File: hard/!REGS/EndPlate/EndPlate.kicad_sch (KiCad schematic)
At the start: 10 parts, among them J1 Conn_01x13_Socket, J2 Conn_01x13_Socket, J3 Conn_01x13_Socket, J4 Conn_01x13_Socket, J5 Conn_01x13_Socket, J6 Conn_01x13_Socket, J7 Conn_01x13_Socket, J8 Conn_01x13_Socket, U1 74HC245, U2 74HC245

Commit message: End Plate PCB in work
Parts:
- added J10, J9: Conn_01x03_Pin, Connector_PinHeader_2.54mm:PinHeader_1x03_P2.54mm_Vertical, symbol Connector:Conn_01x03_Pin
- J1, J2, J3, J4, J5, J6, J7, J8: footprint Connector_PinSocket_2.54mm:PinSocket_1x13_P2.54mm_Vertical -> Connector_PinSocket_2.54mm:PinSocket_1x13_P2.54mm_Vertical_SMD_Pin1Left
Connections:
- net DST0: now also J1.11 (Pin_11); no longer J1.6 (Pin_6)
- net DST1: now also J2.11 (Pin_11); no longer J2.6 (Pin_6)
- net DST2: now also J3.11 (Pin_11); no longer J3.6 (Pin_6)
- net DST3: now also J4.11 (Pin_11); no longer J4.6 (Pin_6)
- net DST4: now also J5.11 (Pin_11); no longer J5.6 (Pin_6)
- net DST5: now also J6.11 (Pin_11); no longer J6.6 (Pin_6)
- net DST6: now also J7.11 (Pin_11); no longer J7.6 (Pin_6)
- net DST7: now also J8.11 (Pin_11); no longer J8.6 (Pin_6)
- net S0.0: now also J9.1 (Pin_1)
- net S0.1: now also J9.2 (Pin_2)
- net S0.2: now also J9.3 (Pin_3)
- net S1.0: now also J1.6 (Pin_6), J2.6 (Pin_6), J3.6 (Pin_6), J4.6 (Pin_6), J5.6 (Pin_6), J6.6 (Pin_6), J7.6 (Pin_6), J8.6 (Pin_6), J10.1 (Pin_1); no longer J1.8 (Pin_8), J2.8 (Pin_8), J3.8 (Pin_8), J4.8 (Pin_8), J5.8 (Pin_8), J6.8 (Pin_8), J7.8 (Pin_8), J8.8 (Pin_8)
- net S1.1: now also J1.7 (Pin_7), J2.7 (Pin_7), J3.7 (Pin_7), J4.7 (Pin_7), J5.7 (Pin_7), J6.7 (Pin_7), J7.7 (Pin_7), J8.7 (Pin_7), J10.2 (Pin_2); no longer J1.9 (Pin_9), J2.9 (Pin_9), J3.9 (Pin_9), J4.9 (Pin_9), J5.9 (Pin_9), J6.9 (Pin_9), J7.9 (Pin_9), J8.9 (Pin_9)
- net S1.2: now also J1.8 (Pin_8), J2.8 (Pin_8), J3.8 (Pin_8), J4.8 (Pin_8), J5.8 (Pin_8), J6.8 (Pin_8), J7.8 (Pin_8), J8.8 (Pin_8), J10.3 (Pin_3); no longer J1.10 (Pin_10), J2.10 (Pin_10), J3.10 (Pin_10), J4.10 (Pin_10), J5.10 (Pin_10), J6.10 (Pin_10), J7.10 (Pin_10), J8.10 (Pin_10)
- net ~E1: now also J1.9 (Pin_9), J2.9 (Pin_9), J3.9 (Pin_9), J4.9 (Pin_9), J5.9 (Pin_9), J6.9 (Pin_9), J7.9 (Pin_9), J8.9 (Pin_9); no longer J1.11 (Pin_11), J2.11 (Pin_11), J3.11 (Pin_11), J4.11 (Pin_11), J5.11 (Pin_11), J6.11 (Pin_11), J7.11 (Pin_11), J8.11 (Pin_11)

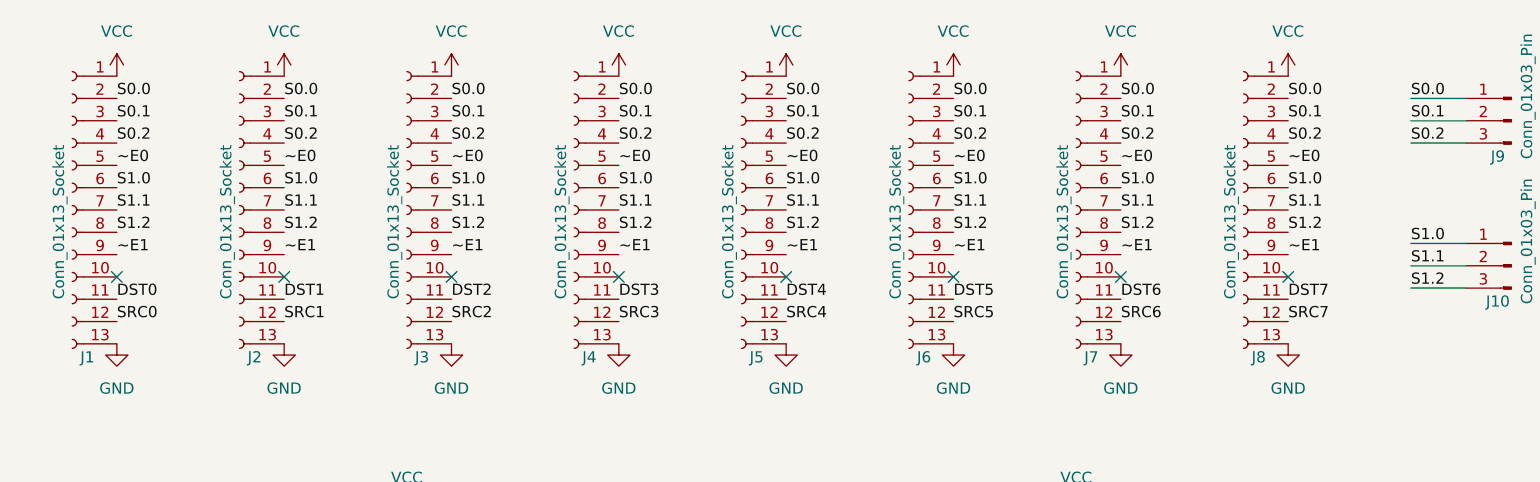
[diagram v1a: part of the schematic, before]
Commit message: End Plate: make a circuit corresponding to the multiplexers
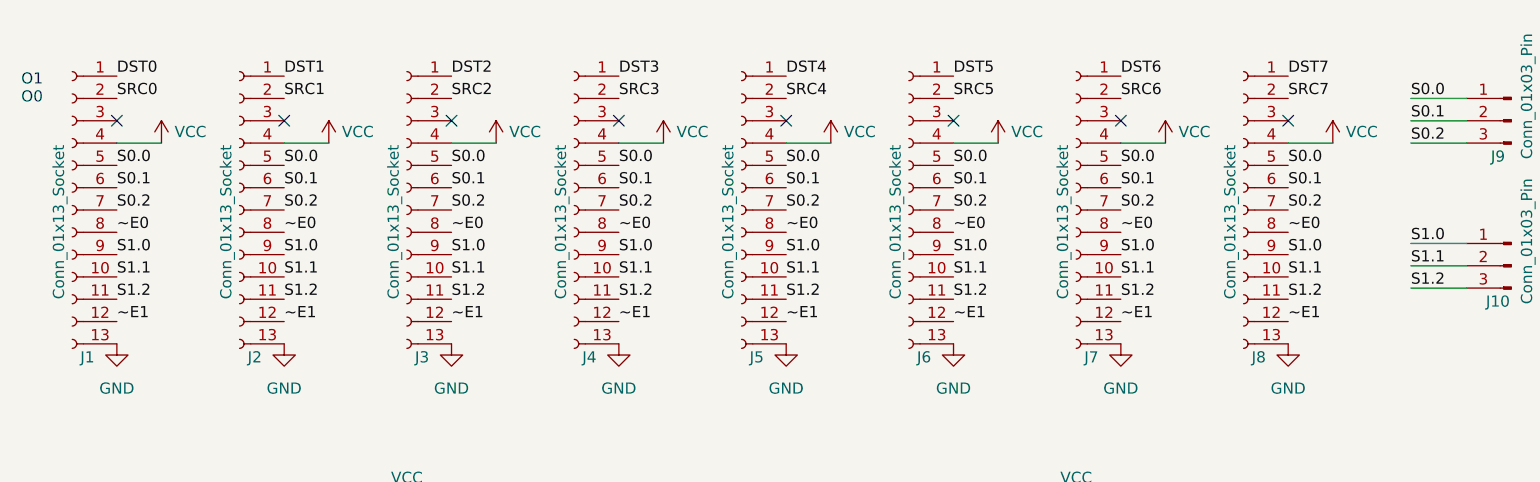
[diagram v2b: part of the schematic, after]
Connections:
- net DST0: now also J1.1 (Pin_1); no longer J1.11 (Pin_11)
- net DST1: now also J2.1 (Pin_1); no longer J2.11 (Pin_11)
- net DST2: now also J3.1 (Pin_1); no longer J3.11 (Pin_11)
- net DST3: now also J4.1 (Pin_1); no longer J4.11 (Pin_11)
- net DST4: now also J5.1 (Pin_1); no longer J5.11 (Pin_11)
- net DST5: now also J6.1 (Pin_1); no longer J6.11 (Pin_11)
- net DST6: now also J7.1 (Pin_1); no longer J7.11 (Pin_11)
- net DST7: now also J8.1 (Pin_1); no longer J8.11 (Pin_11)
- net S0.0: now also J1.5 (Pin_5), J2.5 (Pin_5), J3.5 (Pin_5), J4.5 (Pin_5), J5.5 (Pin_5), J6.5 (Pin_5), J7.5 (Pin_5), J8.5 (Pin_5); no longer J1.2 (Pin_2), J2.2 (Pin_2), J3.2 (Pin_2), J4.2 (Pin_2), J5.2 (Pin_2), J6.2 (Pin_2), J7.2 (Pin_2), J8.2 (Pin_2)
- net S0.1: now also J1.6 (Pin_6), J2.6 (Pin_6), J3.6 (Pin_6), J4.6 (Pin_6), J5.6 (Pin_6), J6.6 (Pin_6), J7.6 (Pin_6), J8.6 (Pin_6); no longer J1.3 (Pin_3), J2.3 (Pin_3), J3.3 (Pin_3), J4.3 (Pin_3), J5.3 (Pin_3), J6.3 (Pin_3), J7.3 (Pin_3), J8.3 (Pin_3)
- net S0.2: now also J1.7 (Pin_7), J2.7 (Pin_7), J3.7 (Pin_7), J4.7 (Pin_7), J5.7 (Pin_7), J6.7 (Pin_7), J7.7 (Pin_7), J8.7 (Pin_7); no longer J1.4 (Pin_4), J2.4 (Pin_4), J3.4 (Pin_4), J4.4 (Pin_4), J5.4 (Pin_4), J6.4 (Pin_4), J7.4 (Pin_4), J8.4 (Pin_4)
- net S1.0: now also J1.9 (Pin_9), J2.9 (Pin_9), J3.9 (Pin_9), J4.9 (Pin_9), J5.9 (Pin_9), J6.9 (Pin_9), J7.9 (Pin_9), J8.9 (Pin_9); no longer J1.6 (Pin_6), J2.6 (Pin_6), J3.6 (Pin_6), J4.6 (Pin_6), J5.6 (Pin_6), J6.6 (Pin_6), J7.6 (Pin_6), J8.6 (Pin_6)
- net S1.1: now also J1.10 (Pin_10), J2.10 (Pin_10), J3.10 (Pin_10), J4.10 (Pin_10), J5.10 (Pin_10), J6.10 (Pin_10), J7.10 (Pin_10), J8.10 (Pin_10); no longer J1.7 (Pin_7), J2.7 (Pin_7), J3.7 (Pin_7), J4.7 (Pin_7), J5.7 (Pin_7), J6.7 (Pin_7), J7.7 (Pin_7), J8.7 (Pin_7)
- net S1.2: now also J1.11 (Pin_11), J2.11 (Pin_11), J3.11 (Pin_11), J4.11 (Pin_11), J5.11 (Pin_11), J6.11 (Pin_11), J7.11 (Pin_11), J8.11 (Pin_11); no longer J1.8 (Pin_8), J2.8 (Pin_8), J3.8 (Pin_8), J4.8 (Pin_8), J5.8 (Pin_8), J6.8 (Pin_8), J7.8 (Pin_8), J8.8 (Pin_8)
- net SRC0: now also J1.2 (Pin_2); no longer J1.12 (Pin_12)
- net SRC1: now also J2.2 (Pin_2); no longer J2.12 (Pin_12)
- net SRC2: now also J3.2 (Pin_2); no longer J3.12 (Pin_12)
- net SRC3: now also J4.2 (Pin_2); no longer J4.12 (Pin_12)
- net SRC4: now also J5.2 (Pin_2); no longer J5.12 (Pin_12)
- net SRC5: now also J6.2 (Pin_2); no longer J6.12 (Pin_12)
- net SRC6: now also J7.2 (Pin_2); no longer J7.12 (Pin_12)
- net SRC7: now also J8.2 (Pin_2); no longer J8.12 (Pin_12)
- net VCC: now also J1.4 (Pin_4), J2.4 (Pin_4), J3.4 (Pin_4), J4.4 (Pin_4), J5.4 (Pin_4), J6.4 (Pin_4), J7.4 (Pin_4), J8.4 (Pin_4); no longer J1.1 (Pin_1), J2.1 (Pin_1), J3.1 (Pin_1), J4.1 (Pin_1), J5.1 (Pin_1), J6.1 (Pin_1), J7.1 (Pin_1), J8.1 (Pin_1)
- net ~E0: now also J1.8 (Pin_8), J2.8 (Pin_8), J3.8 (Pin_8), J4.8 (Pin_8), J5.8 (Pin_8), J6.8 (Pin_8), J7.8 (Pin_8), J8.8 (Pin_8); no longer J1.5 (Pin_5), J2.5 (Pin_5), J3.5 (Pin_5), J4.5 (Pin_5), J5.5 (Pin_5), J6.5 (Pin_5), J7.5 (Pin_5), J8.5 (Pin_5)
- net ~E1: now also J1.12 (Pin_12), J2.12 (Pin_12), J3.12 (Pin_12), J4.12 (Pin_12), J5.12 (Pin_12), J6.12 (Pin_12), J7.12 (Pin_12), J8.12 (Pin_12); no longer J1.9 (Pin_9), J2.9 (Pin_9), J3.9 (Pin_9), J4.9 (Pin_9), J5.9 (Pin_9), J6.9 (Pin_9), J7.9 (Pin_9), J8.9 (Pin_9)
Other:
- note added: "O1 O0"

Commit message: End Plate in work
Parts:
- added C1, C2: 0,1uF, Capacitor_THT:C_Axial_L12.0mm_D6.5mm_P15.00mm_Horizontal, symbol Device:C
- added J11, J12, J13, J14: Conn_01x09_Pin, Connector_PinHeader_2.54mm:PinHeader_1x09_P2.54mm_Vertical, symbol Connector:Conn_01x09_Pin
- added J15, J16: Conn_01x01_Pin, Connector_PinHeader_2.54mm:PinHeader_1x01_P2.54mm_Vertical, symbol Connector:Conn_01x01_Pin
- added R1, R2, R3, R4: 10k, Resistor_SMD:R_0805_2012Metric_Pad1.20x1.40mm_HandSolder, symbol Device:R
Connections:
- net BDST0: now also J11.2 (Pin_2), J14.2 (Pin_2)
- net BDST1: now also J11.3 (Pin_3), J14.3 (Pin_3)
- net BDST2: now also J11.4 (Pin_4), J14.4 (Pin_4)
- net BDST3: now also J11.5 (Pin_5), J14.5 (Pin_5)
- net BDST4: now also J11.6 (Pin_6), J14.6 (Pin_6)
- net BDST5: now also J11.7 (Pin_7), J14.7 (Pin_7)
- net BDST6: now also J11.8 (Pin_8), J14.8 (Pin_8)
- net BDST7: now also J11.9 (Pin_9), J14.9 (Pin_9)
- net BSRC0: now also J12.2 (Pin_2), J13.2 (Pin_2)
- net BSRC1: now also J12.3 (Pin_3), J13.3 (Pin_3)
- net BSRC2: now also J12.4 (Pin_4), J13.4 (Pin_4)
- net BSRC3: now also J12.5 (Pin_5), J13.5 (Pin_5)
- net BSRC4: now also J12.6 (Pin_6), J13.6 (Pin_6)
- net BSRC5: now also J12.7 (Pin_7), J13.7 (Pin_7)
- net BSRC6: now also J12.8 (Pin_8), J13.8 (Pin_8)
- net BSRC7: now also J12.9 (Pin_9), J13.9 (Pin_9)
- net GND: now also C1.2, C2.2, J11.1 (Pin_1), J12.1 (Pin_1), J13.1 (Pin_1), J14.1 (Pin_1), R3.1, R4.1
- net VCC: now also C1.1, C2.1, R1.1, R2.1
- net at U1.1 (A->B): now also R1.2
- net at U1.19 (CE): now also J15.1 (Pin_1), R3.2
- net at U2.1 (A->B): now also R2.2
- net at U2.19 (CE): now also J16.1 (Pin_1), R4.2
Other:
- moved on the sheet: U2

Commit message: Move gerbers to subfolder
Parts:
- added C3: 0,1uF, Capacitor_SMD:C_0805_2012Metric_Pad1.18x1.45mm_HandSolder, symbol Device:C
- added J17: Screw_Terminal_01x02, TerminalBlock_Phoenix:TerminalBlock_Phoenix_MKDS-1,5-2_1x02_P5.00mm_Horizontal, symbol Connector:Screw_Terminal_01x02
- added Q1: IRLML5203, Package_TO_SOT_SMD:SOT-23, symbol Transistor_FET:IRLML5203
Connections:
- net GND: now also C3.2, J17.2 (Pin_2), Q1.1 (G)
- net VCC: now also C3.1, Q1.2 (S)
- new net: J17.1 (Pin_1), Q1.3 (D)

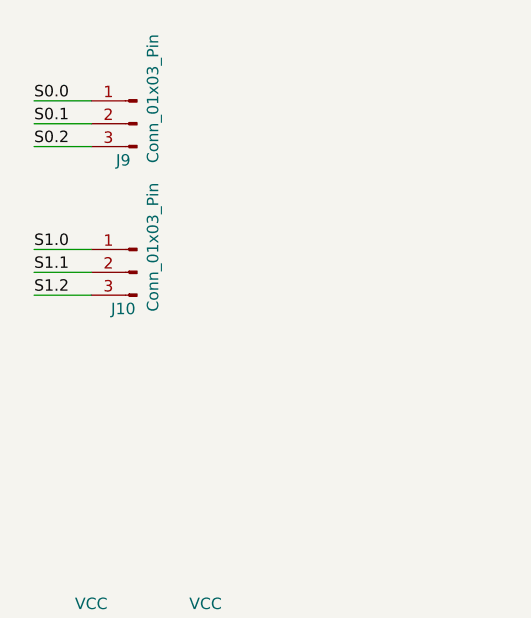
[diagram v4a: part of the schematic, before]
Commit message: End Plate polishing
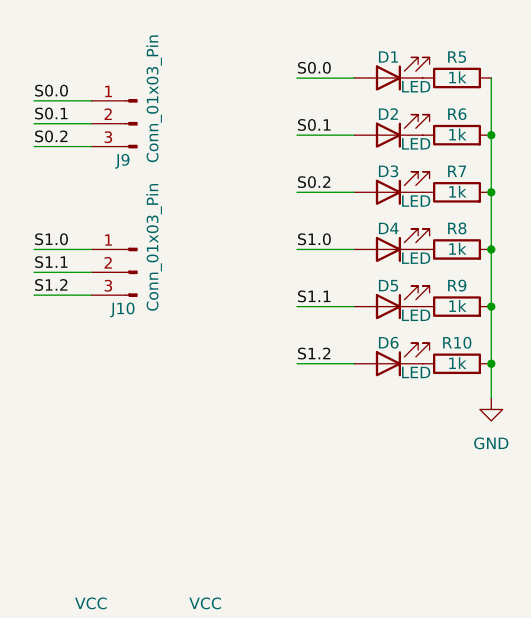
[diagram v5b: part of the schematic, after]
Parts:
- added D1, D2, D3, D4, D5, D6: LED, LED_THT:LED_Rectangular_W5.0mm_H2.0mm, symbol Device:LED
- added R10, R5, R6, R7, R8, R9: 1k, Resistor_SMD:R_0805_2012Metric_Pad1.20x1.40mm_HandSolder, symbol Device:R
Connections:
- net GND: now also R10.2, R5.2, R6.2, R7.2, R8.2, R9.2
- net S0.0: now also D1.2 (A)
- net S0.1: now also D2.2 (A)
- net S0.2: now also D3.2 (A)
- net S1.0: now also D4.2 (A)
- net S1.1: now also D5.2 (A)
- net S1.2: now also D6.2 (A)
- new net: D2.1 (K), R6.1
- new net: D5.1 (K), R9.1
- new net: D4.1 (K), R8.1
- new net: D6.1 (K), R10.1
- new net: D3.1 (K), R7.1
- new net: D1.1 (K), R5.1
